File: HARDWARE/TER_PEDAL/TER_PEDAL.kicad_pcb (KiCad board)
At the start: 2 copper layers, 62 parts, among them J1 DEBUG, J2 APPS_1, J3 RJ45_Shielded, J4 APPS_2, J5 BPPS_1, SW1 RST, U1 STM32F103C8Tx, U2 AOZ1280CI, U3 LM1117MP-3.3, U4 SN65HVD230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

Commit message: Sized and Fixed even more footprints + Initial layout
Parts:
- C11: footprint Capacitor_SMD:C_0603_1608Metric -> Capacitor_SMD:C_1210_3225Metric
- C2, C3, C4, C5, R15: footprint Capacitor_SMD:C_0603_1608Metric -> Capacitor_SMD:C_0402_1005Metric
- C9: footprint Capacitor_SMD:C_Elec_4x5.4 -> Capacitor_SMD:C_1210_3225Metric
- FB1: footprint Inductor_SMD:L_0603_1608Metric -> Inductor_SMD:L_0402_1005Metric
- L1: footprint Inductor_SMD:L_6.3x6.3_H3 -> Inductor_SMD_Wurth:L_Wurth_WE-LQSH-4020
- R13, R14, R6: footprint Resistor_SMD:R_0603_1608Metric -> Resistor_SMD:R_0402_1005Metric
- R3: footprint Resistor_SMD:R_0805_2012Metric -> Resistor_SMD:R_0603_1608Metric
- R8, R9: value 60R -> 50R
- SW1: footprint Button_Switch_SMD:SW_SPST_EVQPE1 -> Button_Switch_SMD:SW_Tactile_SPST_NO_Straight_CK_PTS636Sx25SMTRLFS
- Y1: footprint Crystal:Crystal_HC49-U_Vertical -> Crystal:Crystal_HC52-6mm_Vertical
- moved C3 135.5 mm to (139.2, 91.8), turned to 180 degrees
- moved C5 132.4 mm to (142.5, 83.3), turned to -90 degrees
- moved JP1 128.4 mm to (148.7, 90.6), turned to -90 degrees
- moved C2 126.9 mm to (134.2, 80.4)
- moved C1 126.4 mm to (132.1, 81.0), turned to -90 degrees
- moved JP2 124.3 mm to (148.7, 93.6), turned to -90 degrees
- moved C4 123.2 mm to (130.9, 83.8), turned to -90 degrees
- moved FB1 123.2 mm to (129.9, 88.3), turned to -90 degrees
- moved R4 121.9 mm to (146.2, 88.1), turned to 180 degrees
- moved R5 118.9 mm to (145.9, 95.8), turned to 180 degrees
- moved C7 117.9 mm to (130.9, 87.4), turned to 90 degrees
- moved C6 116.2 mm to (128.2, 87.7), turned to 180 degrees
- moved C15 115.8 mm to (125.8, 80.1)
- moved C8 115.1 mm to (128.2, 88.8), turned to 180 degrees
- moved C16 114.2 mm to (122.6, 80.1)
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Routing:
- net GND: track 0.00 -> 25.9 mm, vias 0 -> 3
- net /CAN/CAN-: track 0.00 -> 18.5 mm
- net /CAN/CAN+: track 0.00 -> 18.3 mm
- net /MICRO/BOOT0: track 0.00 -> 12.7 mm, vias 0 -> 2
- net /CAN/VREF: track 0.00 -> 12.4 mm, vias 0 -> 2
- net /CAN/CAN_TX: track 0.00 -> 12.0 mm
- net /MICRO/BOOT1: track 0.00 -> 11.2 mm
- net /CAN/CAN_RX: track 0.00 -> 11.1 mm
- net Net-(C16-Pad1): track 0.00 -> 10.4 mm
- net /MICRO/OSC_IN: track 0.00 -> 9.99 mm
- net +3.3V: track 0.00 -> 9.54 mm
- net /MICRO/SWDIO: track 0.00 -> 7.09 mm
- net +3.3VADC: track 0.00 -> 4.06 mm
- net Net-(SW1-B): track 0.00 -> 3.45 mm
- net /MICRO/SWCLK: track 0.00 -> 3.09 mm
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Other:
- board outline added: 87.5 x 40 mm

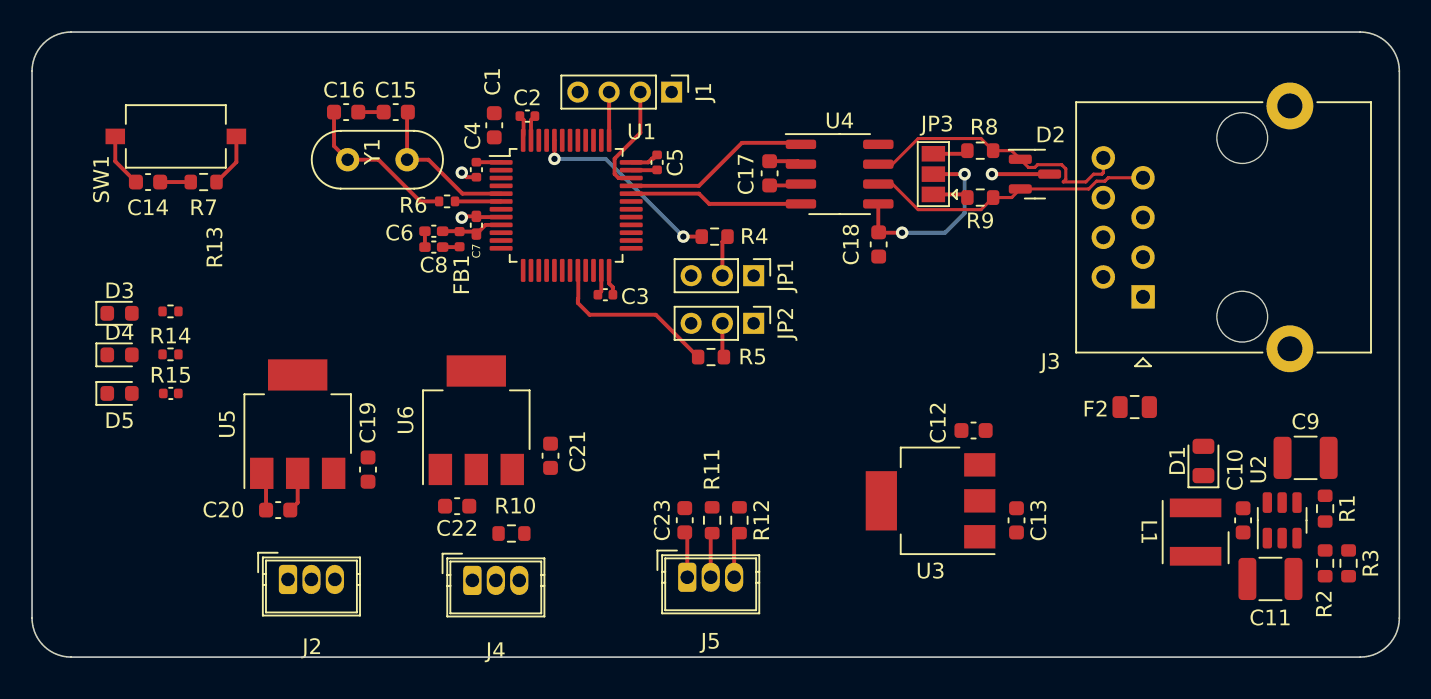
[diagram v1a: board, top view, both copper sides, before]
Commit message: Added Eracing Logo
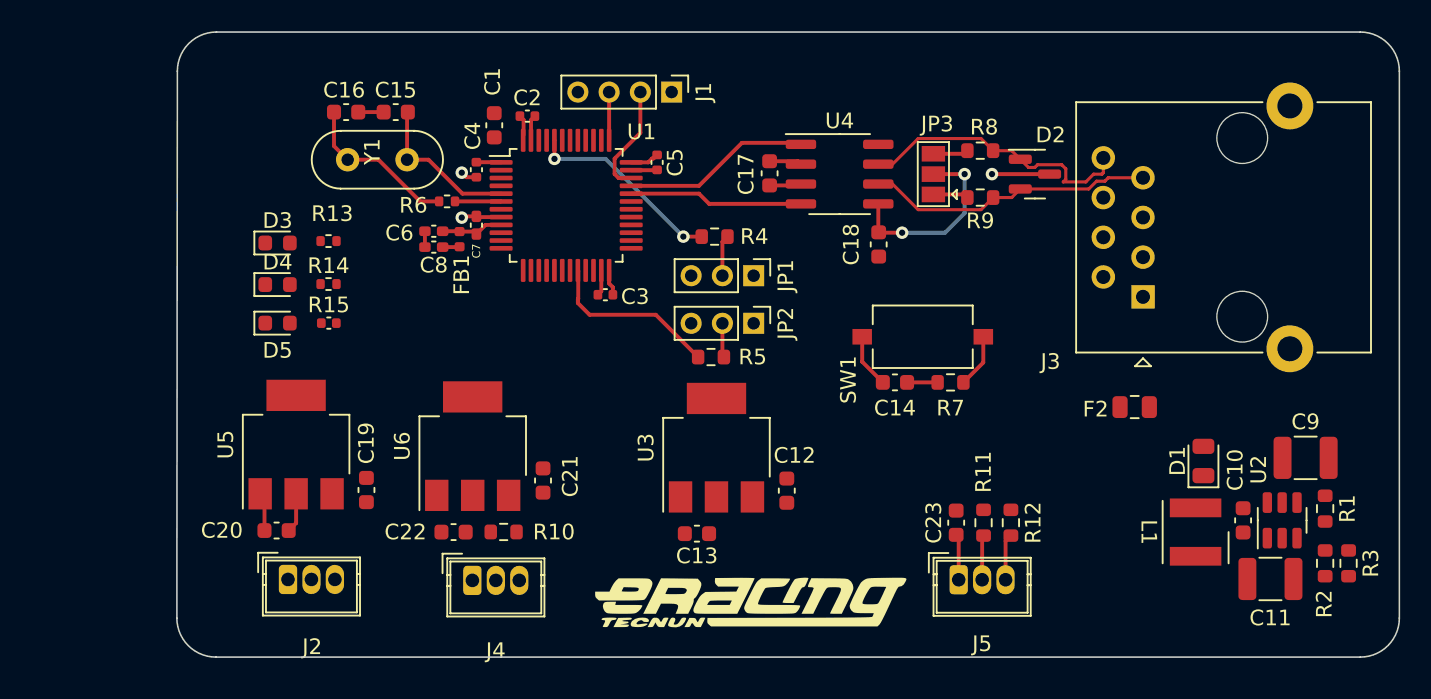
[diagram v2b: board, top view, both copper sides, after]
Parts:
- added G***: LOGO, Logo:eracingLogo, F.Cu at (148.5, 111.5)
- moved C14 49.5 mm to (157.7, 97.4)
- moved R7 49.5 mm to (161.3, 97.4)
- moved SW1 49.5 mm to (159.5, 94.5)
- moved C13 20.5 mm to (145.1, 107.1), turned to 180 degrees
- moved J5 17.4 mm to (161.8, 110.0)
- moved C23 17.4 mm to (161.6, 106.4)
- moved R11 17.4 mm to (163.4, 106.4)
- moved R12 17.4 mm to (165.1, 106.4)
- moved U3 14.1 mm to (146.3, 101.6), turned to 90 degrees
- moved C12 12.6 mm to (150.8, 104.3), turned to 90 degrees
- moved D3 11.1 mm to (118.2, 88.5)
- moved D4 11.1 mm to (118.2, 91.2)
- moved D5 11.1 mm to (118.2, 93.6)
- moved R15 11.1 mm to (121.5, 93.6)
- moved R13 11.1 mm to (121.5, 88.4)
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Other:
- board size 87.5 x 40 mm -> 78.2 x 40 mm

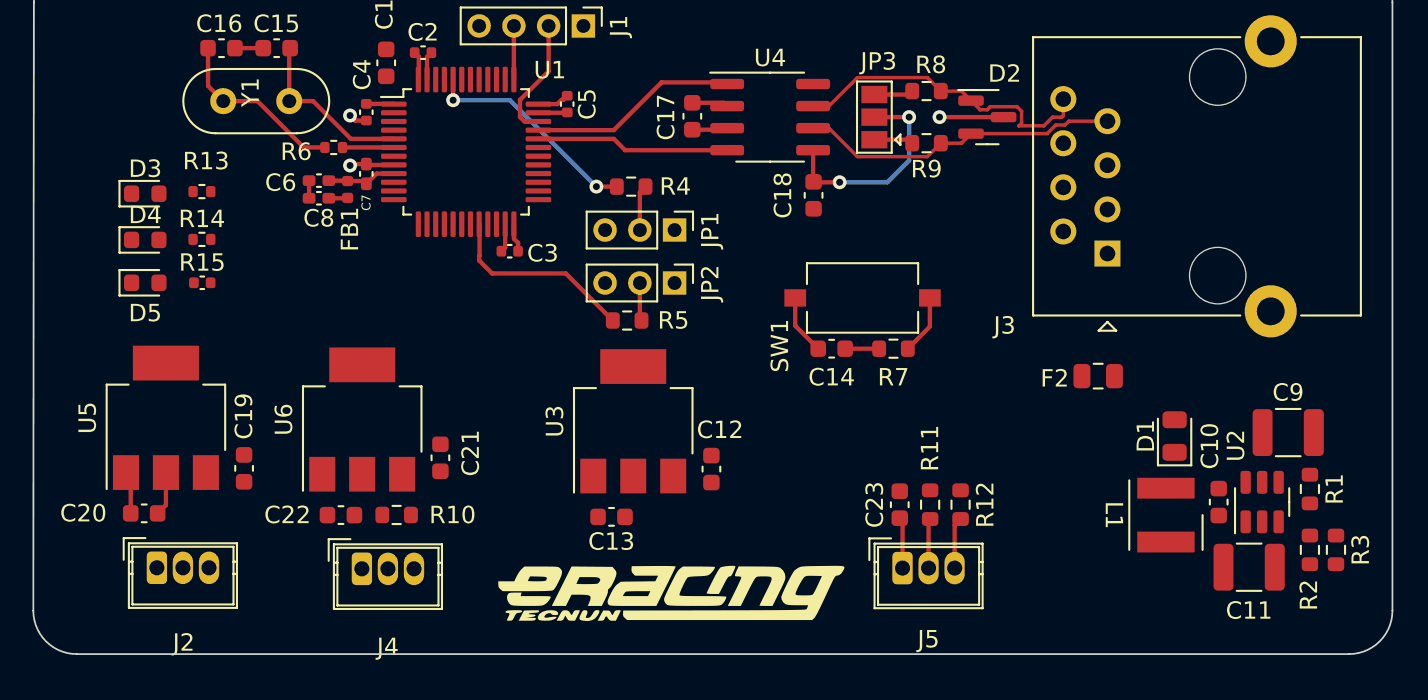
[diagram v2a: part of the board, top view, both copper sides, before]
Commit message: Began layout and switched to 4 layer board
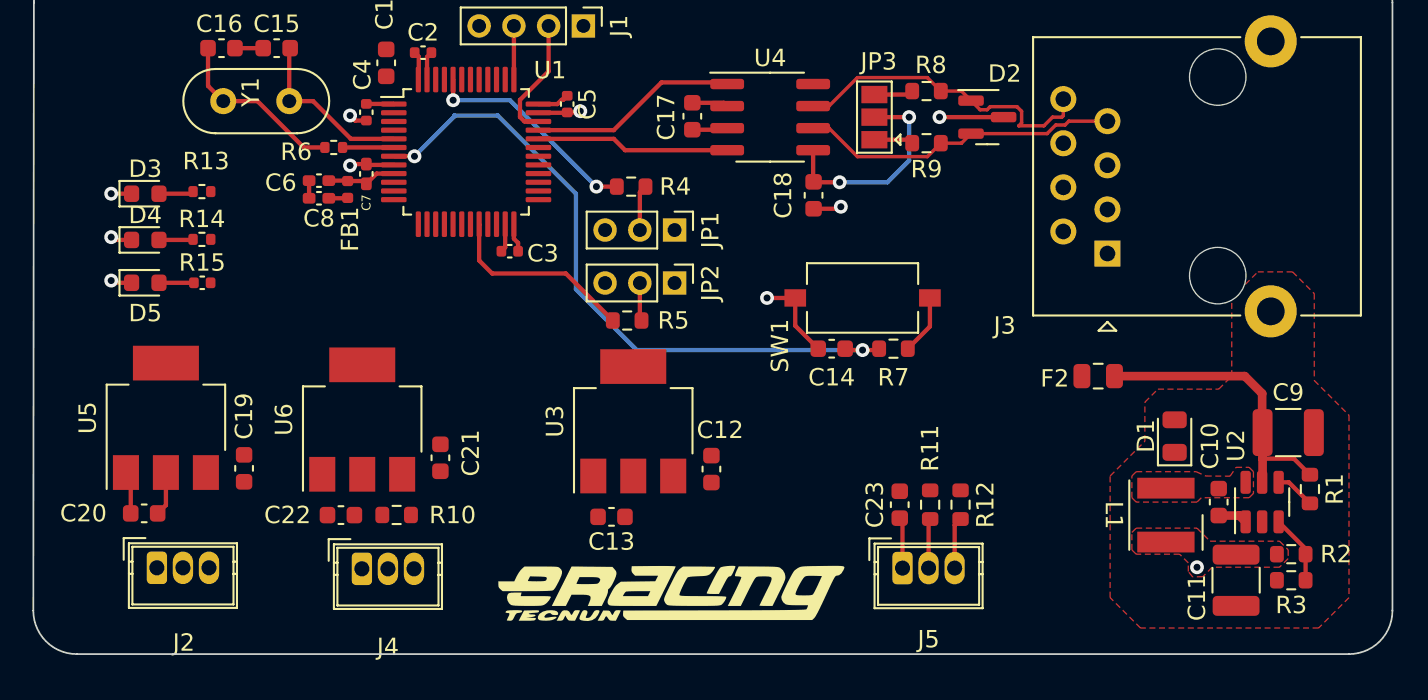
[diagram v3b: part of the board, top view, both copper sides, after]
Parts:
- moved R3 3.11 mm to (184.2, 110.8), turned to 180 degrees
- moved R2 1.10 mm to (184.2, 109.2), turned to 0 degrees
- moved C11 1.06 mm to (181.0, 110.8), turned to -90 degrees
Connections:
- net Net-(D1-K) renamed /POWER/SWTCH
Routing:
- net /MICRO/NRST: track 1.96 -> 38.8 mm, vias 0 -> 2
- net Net-(#FLG02-pwr): track 0.00 -> 17.2 mm
- net GND: track 25.9 -> 33.6 mm, vias 3 -> 9
- net /POWER/FeedBack: track 0.00 -> 4.00 mm
- net Net-(U2-EN): track 0.00 -> 2.30 mm
- net Net-(D3-A): track 0.00 -> 2.01 mm
- net Net-(D5-A): track 0.00 -> 2.01 mm
- net Net-(D4-A): track 0.00 -> 1.98 mm
- net Net-(U2-BST): track 0.00 -> 1.70 mm
- net +5V: vias 0 -> 1
- added copper zone on F.Cu, net +5V
- added copper zone on F.Cu, net /POWER/SWTCH
- added copper zone on F.Cu, net GND
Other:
- copper layers 2 -> 4

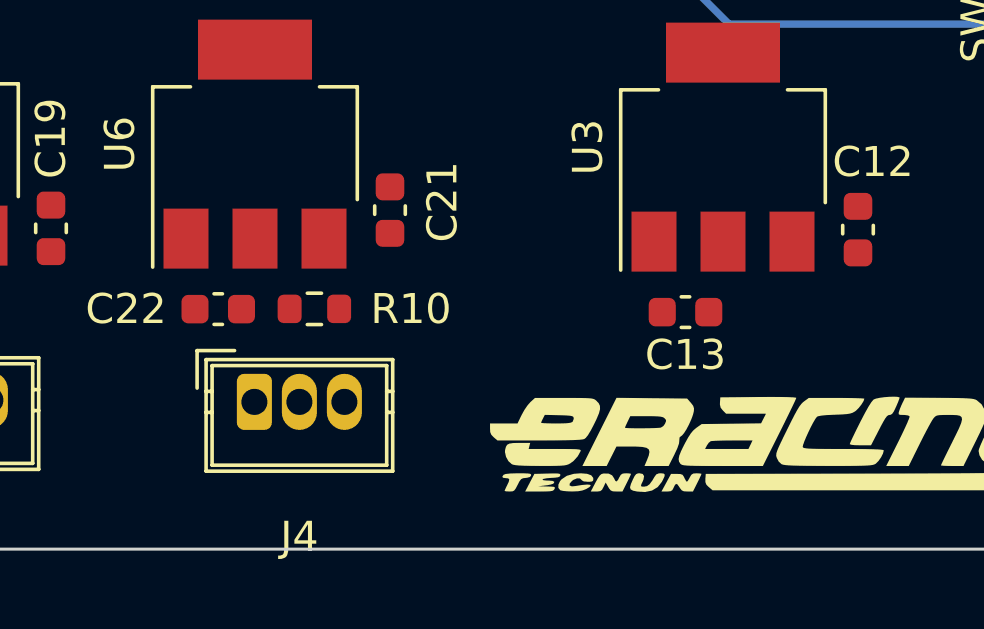
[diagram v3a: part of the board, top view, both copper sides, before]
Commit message: added powerplanes
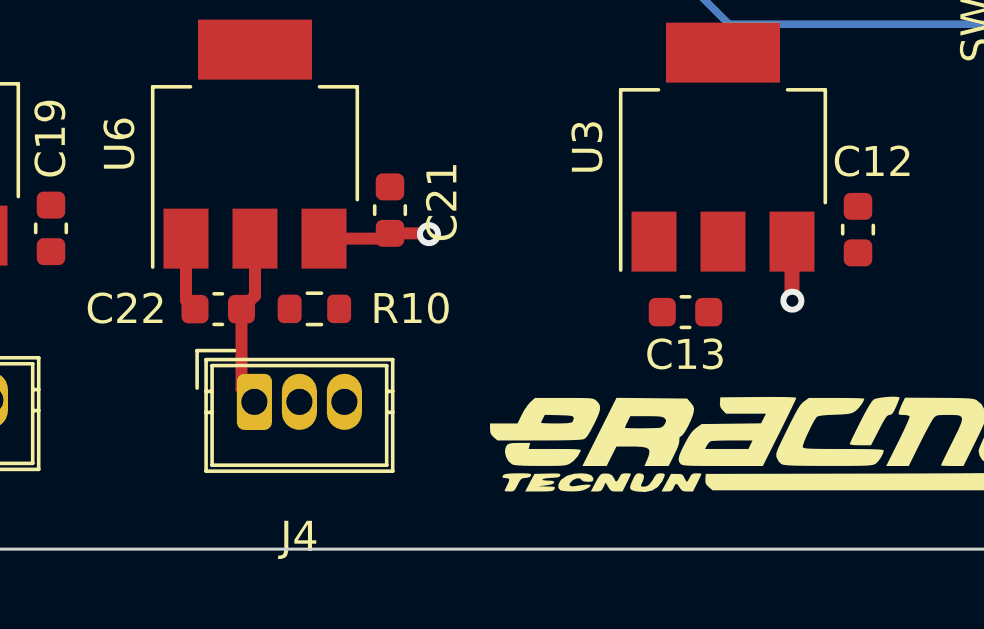
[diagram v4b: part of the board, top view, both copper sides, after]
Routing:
- net /SENSORS/VCC_2: track 0.00 -> 5.81 mm
- net +5V: track 2.94 -> 8.50 mm, vias 1 -> 3
- net GND: track 33.6 -> 36.0 mm
- added copper zone on In2.Cu, net +3.3V
- added copper zone on In2.Cu, net +5V
- added copper zone on In1.Cu, net GND
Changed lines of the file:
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@@
   (layers
     (0 "F.Cu" signal)
-    (1 "In1.Cu" signal)
-    (2 "In2.Cu" signal)
+    (1 "In1.Cu" power "GND")
+    (2 "In2.Cu" power "PWR")
     (31 "B.Cu" signal)
     (32 "B.Adhes" user "B.Adhesive")
@@
   (segment (start 117.375 104.825) (end 117.1 104.55) (width 0.25) (layer "F.Cu") (net 2))
   (segment (start 123.375 80.123) (end 125 80.123) (width 0.25) (layer "F.Cu") (net 2))
+  (segment (start 128.4 104.65) (end 128.4 106.7) (width 0.4) (layer "F.Cu") (net 2))
   (segment (start 130.29 84.29) (end 130 84) (width 0.25) (layer "F.Cu") (net 2))
   (segment (start 149.7 83.267) (end 151.515 83.267) (width 0.25) (layer "F.Cu") (net 2))
@@
   (segment (start 142.5 83.822) (end 143.178 83.822) (width 0.25) (layer "F.Cu") (net 2))
   (segment (start 130.984 86.842) (end 132.5175 86.842) (width 0.25) (layer "F.Cu") (net 2))
+  (segment (start 128.4 106.7) (end 128.7 107) (width 0.4) (layer "F.Cu") (net 2))
   (segment (start 156.947 97.421) (end 155.625 96.099) (width 0.25) (layer "F.Cu") (net 2))
   (segment (start 167.6175 84.092) (end 163.93 84.092) (width 0.25) (layer "F.Cu") (net 2))
@@
   (segment (start 180 107.025) (end 181.1875 107.025) (width 0.5) (layer "F.Cu") (net 4))
   (segment (start 181.1875 107.025) (end 181.55 107.3875) (width 0.5) (layer "F.Cu") (net 4))
+  (segment (start 148.6 106.705894) (end 148.613068 106.718962) (width 0.5) (layer "F.Cu") (net 6))
+  (segment (start 135.2 104.475) (end 136.475 104.475) (width 0.4) (layer "F.Cu") (net 6))
+  (segment (start 136.475 104.475) (end 136.5 104.5) (width 0.4) (layer "F.Cu") (net 6))
+  (segment (start 135.025 104.65) (end 135.2 104.475) (width 0.4) (layer "F.Cu") (net 6))
+  (segment (start 133 104.65) (end 135.025 104.65) (width 0.4) (layer "F.Cu") (net 6))
   (segment (start 161.8 110.05) (end 161.8 107.335) (width 0.25) (layer "F.Cu") (net 6))
   (segment (start 161.8 107.335) (end 161.64 107.175) (width 0.25) (layer "F.Cu") (net 6))
+  (segment (start 148.6 104.75) (end 148.6 106.705894) (width 0.5) (layer "F.Cu") (net 6))
+  (via (at 136.5 104.5) (size 0.8) (drill 0.4) (layers "F.Cu" "B.Cu") (net 6))
+  (via (at 148.613068 106.718962) (size 0.8) (drill 0.4) (layers "F.Cu" "B.Cu") (net 6))
   (via (at 178.75 110) (size 0.8) (drill 0.4) (layers "F.Cu" "B.Cu") (free) (net 6))
   (segment (start 133.70287 86.342) (end 133.707429 86.346559) (width 0.25) (layer "F.Cu") (net 7))
@@
   (segment (start 119.4 106.425) (end 119.4 104.55) (width 0.25) (layer "F.Cu") (net 11))
   (segment (start 118.925 106.9) (end 119.4 106.425) (width 0.25) (layer "F.Cu") (net 11))
+  (segment (start 130.25 109.662) (end 130.68 110.092) (width 0.4) (layer "F.Cu") (net 12))
+  (segment (start 130.7 104.65) (end 130.7 106.55) (width 0.4) (layer "F.Cu") (net 12))
+  (segment (start 130.7 106.55) (end 130.25 107) (width 0.4) (layer "F.Cu") (net 12))
+  (segment (start 130.25 107) (end 130.25 109.662) (width 0.4) (layer "F.Cu") (net 12))
   (segment (start 157.565 83.457) (end 156.655 83.457) (width 0.2) (layer "F.Cu") (net 13))
   (segment (start 170.433687 84.095019) (end 170.966782 84.095019) (width 0.2) (layer "F.Cu") (net 13))
@@
       )
     )
+  )
+  (zone (net 2) (net_name "GND") (layer "In1.Cu") (hatch edge 0.5)
+    (connect_pads (clearance 0.2))
+    (min_thickness 0.25) (filled_areas_thickness no)
+    (fill yes (thermal_gap 0.5) (thermal_bridge_width 0.5))
+    (polygon
+      (pts
+        (xy 113.25 113.5)
+        (xy 189 113.5)
+        (xy 189 76.75)
+        (xy 188.75 76.5)
+        (xy 113.25 76.5)
+      )
+    )
+  )
+  (zone (net 1) (net_name "+3.3V") (layer "In2.Cu") (hatch edge 0.5)
+    (priority 4)
+    (connect_pads (clearance 0.2))
+    (min_thickness 0.25) (filled_areas_thickness no)
+    (fill yes (thermal_gap 0.5) (thermal_bridge_width 0.5))
+    (polygon
+      (pts
+        (xy 113.25 76.5)
+        (xy 113.25 101.5)
+        (xy 165.25 101.5)
+        (xy 168.75 101.5)
+        (xy 168.75 76.5)
+      )
+    )
+  )
+  (zone (net 6) (net_name "+5V") (layer "In2.Cu") (hatch edge 0.5)
+    (priority 5)
+    (connect_pads (clearance 0.2))
+    (min_thickness 0.25) (filled_areas_thickness no)
+    (fill yes (thermal_gap 0.5) (thermal_bridge_width 0.5))
+    (polygon
+      (pts
+        (xy 113.25 113.5)
+        (xy 189 113.5)
+        (xy 189 102)
+        (xy 113.25 102)
+      )
+    )

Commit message: Initial Layout Finished
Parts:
- moved F2 4.71 mm to (177.8, 98.5)
- moved C9 3.26 mm to (180.8, 102.5), turned to 180 degrees
- moved R1 3.25 mm to (184.0, 102.5)
- moved D3 2.50 mm to (118.2, 91.0)
- moved R13 2.50 mm to (121.5, 90.9)
- moved D4 2.41 mm to (118.2, 88.8)
- moved R14 2.41 mm to (121.5, 88.7)
- moved D1 1.25 mm to (176.2, 102.8)
- moved D2 0.43 mm to (166.2, 84.1)
- moved JP3 0.43 mm to (159.8, 84.1)
- moved R8 0.43 mm to (162.8, 82.6)
- moved R9 0.43 mm to (162.8, 85.6)
- moved D5 0.38 mm to (118.2, 93.2)
- moved R15 0.38 mm to (121.5, 93.2)
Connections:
- U1 pad 10: /SENSORS/SENS_1 -> unconnected-(U1-PA0-Pad10)
- U1 pad 11: /MICRO/APPS_2_ADC -> unconnected-(U1-PA1-Pad11)
- U1 pad 12: /MICRO/BPPS_ADC -> unconnected-(U1-PA2-Pad12)
- U1 pad 13: unconnected-(U1-PA3-Pad13) -> /IMP_LED
- U1 pad 14: unconnected-(U1-PA4-Pad14) -> /DBG_LED
- U1 pad 16: unconnected-(U1-PA6-Pad16) -> /SENSORS/SENS_1
- U1 pad 17: unconnected-(U1-PA7-Pad17) -> /MICRO/APPS_2_ADC
- U1 pad 19: unconnected-(U1-PB1-Pad19) -> /MICRO/BPPS_ADC
- U1 pad 39: /IMP_LED -> unconnected-(U1-PB3-Pad39)
- U1 pad 40: /DBG_LED -> unconnected-(U1-PB4-Pad40)
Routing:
- net /MICRO/BPPS_ADC: track 0.00 -> 36.1 mm
- net GND: track 36.0 -> 67.4 mm, vias 9 -> 31
- net /SENSORS/SENS_1: track 0.00 -> 29.5 mm
- net +24V: track 0.00 -> 20.8 mm
- net /MICRO/APPS_2_ADC: track 0.00 -> 20.3 mm
- net +3.3V: track 9.54 -> 28.8 mm, vias 0 -> 8
- net /DBG_LED: track 0.00 -> 13.5 mm
- net /IMP_LED: track 0.00 -> 12.6 mm
- net +5V: track 8.50 -> 15.0 mm, vias 3 -> 4
- net /SENSORS/VCC_2: track 5.81 -> 12.1 mm
- net /SENSORS/VCC_1: track 2.55 -> 8.85 mm
- net Net-(U2-VIN): track 17.2 -> 11.7 mm
- net /SENSORS/SENS_2: track 0.00 -> 3.23 mm
- net /CAN/CAN+: track 18.3 -> 19.2 mm
- net /CAN/CAN-: track 18.5 -> 19.4 mm
- removed copper zone on F.Cu, net GND
